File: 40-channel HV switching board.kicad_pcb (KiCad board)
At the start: 2 copper layers, 83.8 x 121.9 mm, 210 parts, among them IC1 ATMEG328PU, J1 CONN_4, J2 CONN_10, J3 CONN_2, J4 CONN_2, J5 CONN_40, P1 CONN_6, P2 CONN_6, SW1 DPST, U1 74HC595A, U2 74HC595A, U3 74HC595A, U4 74HC595A, U5 74HC595A, U6 7400, X1 16MHz

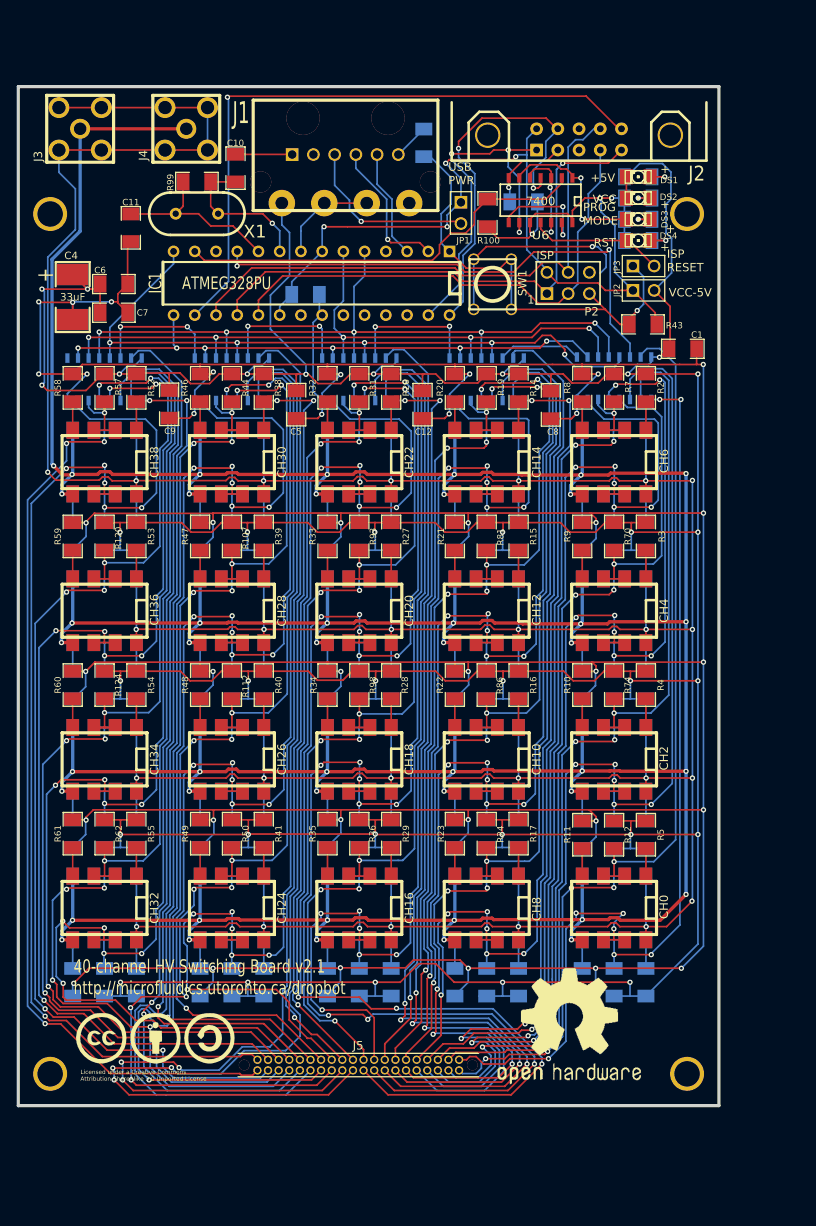
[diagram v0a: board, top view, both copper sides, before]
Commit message: Update to work with KiCad 4.0
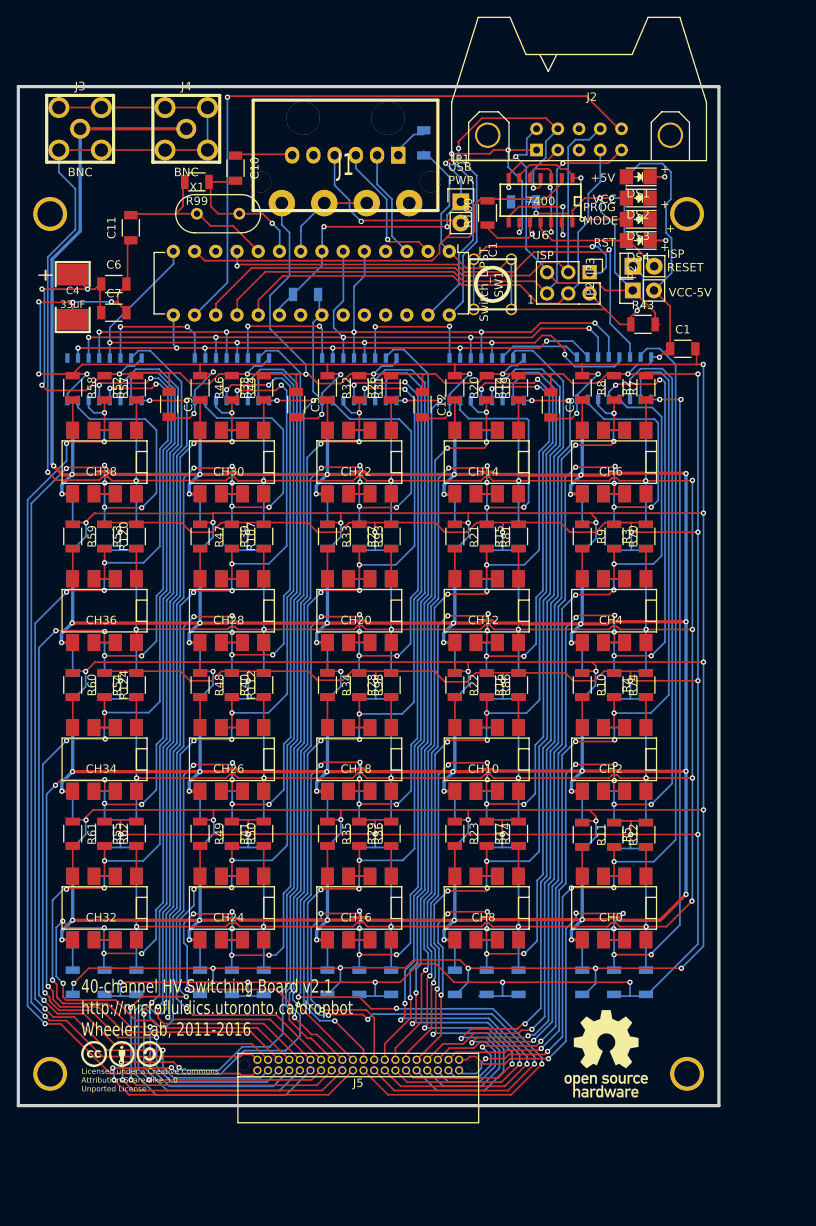
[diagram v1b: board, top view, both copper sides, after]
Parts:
- removed the G*** at (33.0, 129.1)
- removed the G*** at (72.9, 118.4)
- added G***: LOGO, footprints:OSHW_logo_10mm, F.Cu at (86.8, 130.9)
- added G***: LOGO, footprints:CC_S_A_logo_10mm, F.Cu at (28.9, 130.9)
- C1, C10, C11, C12, C13, C14, C3, C5, C6, C7, C8, C9: footprint SM1206 -> Capacitors_SMD:C_1206
- C2, C4: footprint SM2917 -> footprints:SM2917
- CH0, CH1, CH10, CH11, CH12, CH13, CH14, CH15, CH16, CH17, CH18, CH19, CH2, CH20, CH21, CH22, CH23, CH24, CH25, CH26, CH27, CH28, CH29, CH3, CH30, CH31, CH32, CH33, CH34, CH35, CH36, CH37, CH38, CH39, CH4, CH5, CH6, CH7, CH8, CH9: footprint 8DIPCMS -> SMD_Packages:DIP-8_SMD
- DS1, DS2, DS3, DS4: footprint LED-1206 -> LEDs:LED_1206
- IC1: footprint DIP-28 -> Housings_DIP:DIP-28_W7.62mm
- J1: value CONN_4 -> CONN_01X04; footprint Molex_15-24-4441 -> footprints:Molex_15-24-4441
- J2: value CONN_10 -> CONN_01X10; footprint HE10-10C -> Connect:HE10-10C
- J3, J4: value CONN_2 -> BNC; footprint JACK_SMA -> footprints:JACK_SMA
- J5: value CONN_40 -> CONN_01X40; footprint TFML-120-01-XXX-D-RA -> footprints:TFML-120-01-XXX-D-RA
- JP1, JP2, JP3: footprint PIN_ARRAY_2X1 -> Pin_Headers:Pin_Header_Straight_1x02
- P1: value CONN_6 -> CONN_01X06; footprint PIN_ARRAY-6X1 -> Pin_Headers:Pin_Header_Angled_1x06
- P2: value CONN_6 -> CONN_01X06; footprint pin_array_3x2 -> Pin_Headers:Pin_Header_Straight_2x03
- R1, R10, R100, R101, R102, R103, R104, R105, R106, R107, R108, R109, R11, R110, R111, R112, R113, R114, R115, R116, R117, R118, R119, R12, R120, R121, R122, R123, R124, R125, R126, R127, R13, R14, R15, R16, R17, R18, R19, R2, R20, R21, R22, R23, R24, R25, R26, R27, R28, R29, R3, R30, R31, R32, R33, R34, R35, R36, R37, R38, R39, R4, R40, R41, R42, R43, R44, R45, R46, R47, R48, R49, R5, R50, R51, R52, R53, R54, R55, R56, R57, R58, R59, R6, R60, R61, R62, R63, R64, R65, R66, R67, R68, R69, R7, R70, R71, R72, R73, R74, R75, R76, R77, R78, R79, R8, R80, R81, R82, R83, R84, R85, R86, R87, R88, R89, R9, R90, R91, R92, R93, R94, R95, R96, R97, R98, R99: footprint SM1206 -> Resistors_SMD:R_1206
- SW1: value DPST -> Switch_DPST; footprint SW_PUSH_6mm -> footprints:SW_PUSH_6mm
- U1, U2, U3, U4, U5: footprint SO16E -> footprints:SO16E
- U6: footprint SO14E -> footprints:SO14E
- X1: footprint HC-49V -> Crystals:HC-49V
- moved IC1 16.9 mm to (68.1, 35.0), turned to 270 degrees
- moved P1 6.35 mm to (62.0, 23.4), turned to 90 degrees
- moved P2 2.86 mm to (84.8, 37.5), turned to 270 degrees
- moved JP1 1.33 mm to (69.5, 29.0), turned to 0 degrees
- moved JP2 1.29 mm to (90.0, 39.6), turned to 90 degrees
- moved JP3 1.26 mm to (90.0, 36.7), turned to 90 degrees
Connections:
- C3 pad 1: N-00000115 -> Net-(C3-Pad1)
- IC1 pad 12: (no net) -> Net-(IC1-Pad12)
- IC1 pad 21: (no net) -> Net-(IC1-Pad21)
- IC1 pad 23: (no net) -> Net-(IC1-Pad23)
- IC1 pad 24: (no net) -> Net-(IC1-Pad24)
- IC1 pad 25: (no net) -> Net-(IC1-Pad25)
- IC1 pad 26: (no net) -> Net-(IC1-Pad26)
- IC1 pad 4: (no net) -> Net-(IC1-Pad4)
- J1 pad 1: (no net) -> Net-(J1-Pad1)
- J2 pad 5: (no net) -> Net-(J2-Pad5)
- J2 pad 6: (no net) -> Net-(J2-Pad6)
- J3 pad 1: HVGND -> HV
- J3 pad 2: HV -> HVGND
- J4 pad 1: HVGND -> HV
- J4 pad 2: HV -> HVGND
- P1 pad 1: GND -> Net-(C3-Pad1)
- P1 pad 2: (no net) -> RX
- P1 pad 3: +5V_USB -> TX
- P1 pad 4: TX -> +5V_USB
- P1 pad 5: RX -> Net-(P1-Pad5)
- P1 pad 6: N-00000115 -> GND
- P2 pad 1: D12/MISO -> GND
- P2 pad 2: VCC -> RST
- P2 pad 3: D13/SCK -> D11/MOSI
- P2 pad 4: D11/MOSI -> D13/SCK
- P2 pad 5: RST -> VCC
- P2 pad 6: GND -> D12/MISO
- U5 pad 9: (no net) -> Net-(U5-Pad9)
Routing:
- net Net-(C3-Pad1): track 0.00 -> 4.44 mm
- net N-00000115: track 4.31 -> 0.00 mm
- net D7: track 50.3 -> 52.1 mm
- net VCC: track 126.4 -> 125.4 mm, vias 7 -> 8
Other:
- board text added: "40-channel HV Switching Board v2.1 http://microfluidics.utoronto.ca/dropbot Wheeler Lab, 2011-2016"
- board text removed: "40-channel HV Switching Board v2.1 http://microfluidics.utoronto.ca/dropbot"

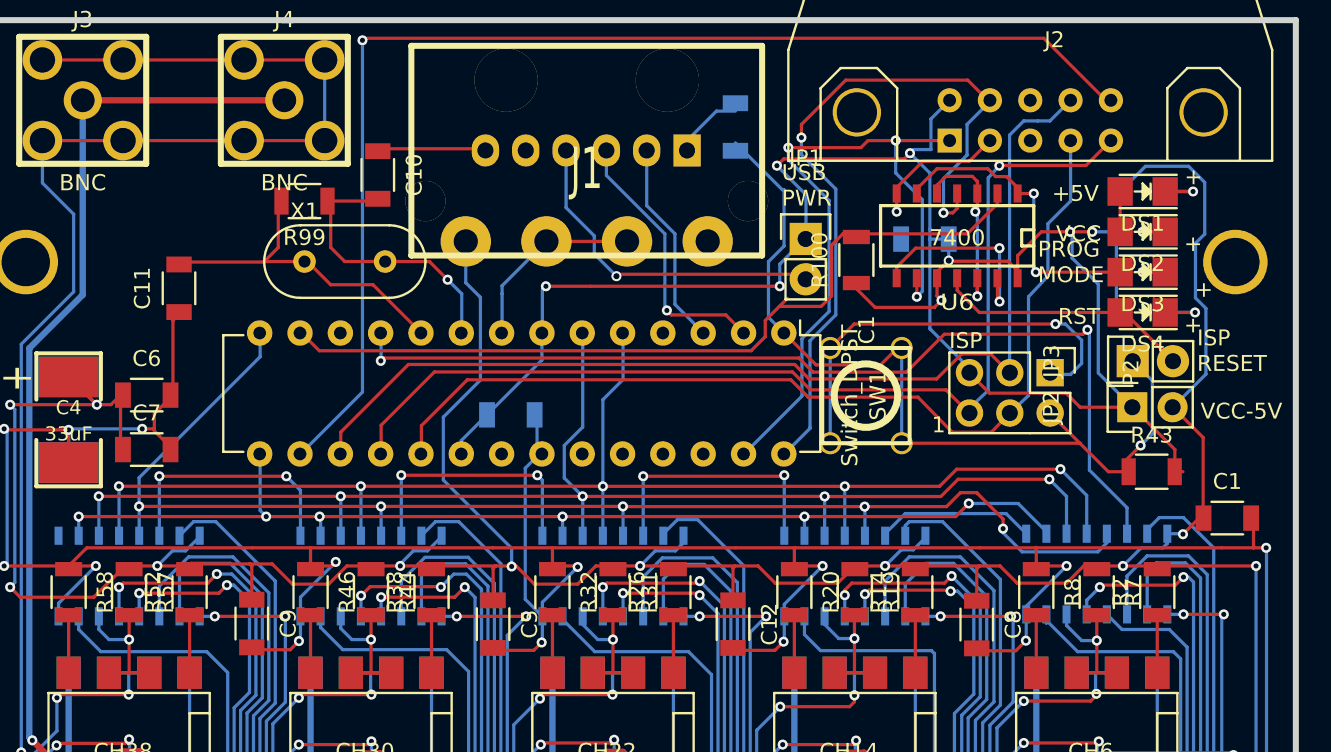
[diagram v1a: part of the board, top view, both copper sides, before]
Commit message: [WIP] Switch caps and LEDs to 0805 footprints
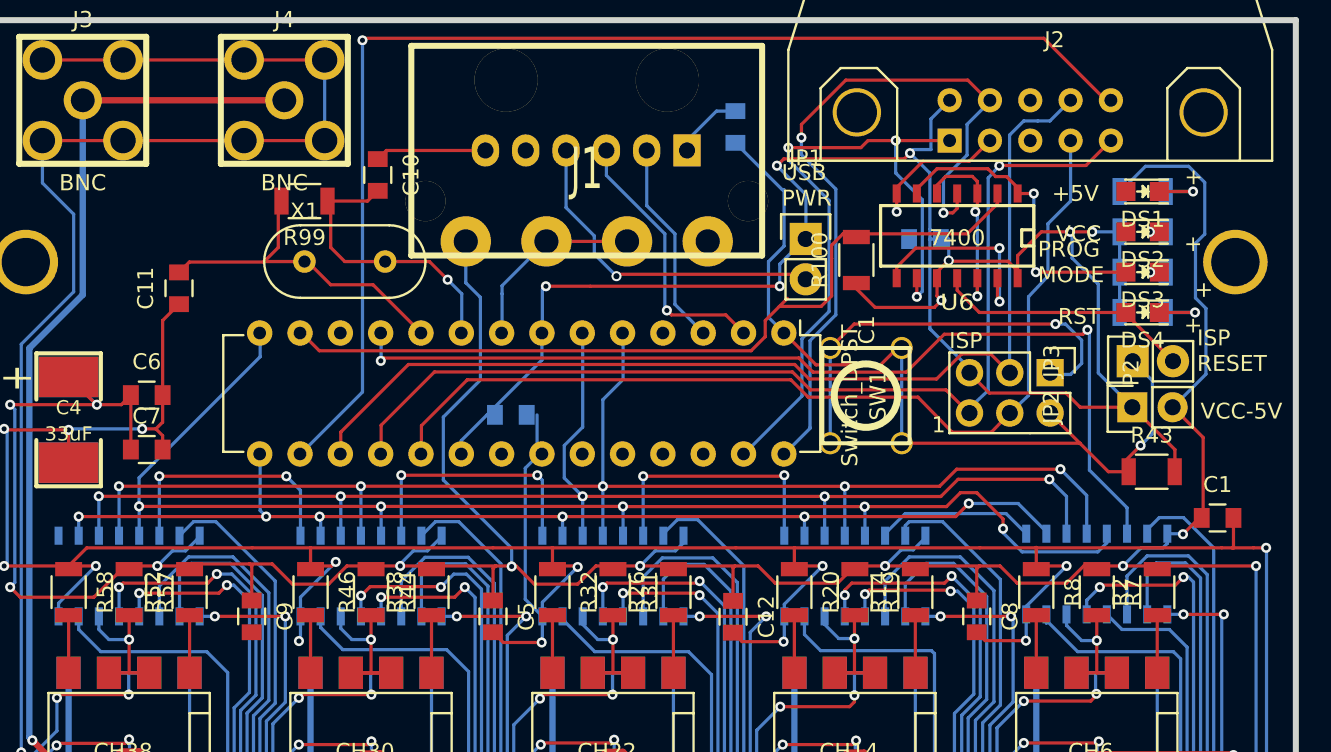
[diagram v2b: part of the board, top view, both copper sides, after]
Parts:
- C1, C10, C11, C12, C13, C14, C3, C5, C6, C7, C8, C9: footprint Capacitors_SMD:C_1206 -> Capacitors_SMD:C_0805
- DS1, DS2, DS3, DS4: footprint LEDs:LED_1206 -> LEDs:LED_0805
- moved C1 0.61 mm to (95.4, 46.6)
- moved C8 0.51 mm to (80.2, 52.8)
- moved C5 0.49 mm to (49.8, 52.8)
- moved C12 0.46 mm to (64.9, 52.8)
- moved C9 0.45 mm to (34.5, 52.8)
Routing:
- net GND: track 728.0 -> 723.0 mm
- net Net-(DS3-Pad1): track 3.07 -> 1.56 mm
- net Net-(DS2-Pad1): track 3.07 -> 1.61 mm
- net +5V: track 712.6 -> 714.0 mm

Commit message: [WIP] Add sci-bots logo
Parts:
- added G***: LOGO, LOGO, F.Cu at (34.0, 120.9)
- moved G*** 0.83 mm to (28.8, 131.8)
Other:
- board text added: "40-channel HV Switching Board v2.1 http://sci-bots.com Sci-Bots Inc., 2016"
- board text removed: "40-channel HV Switching Board v2.1 http://microfluidics.utoronto.ca/dropbot Wheeler Lab, 2011-2016"

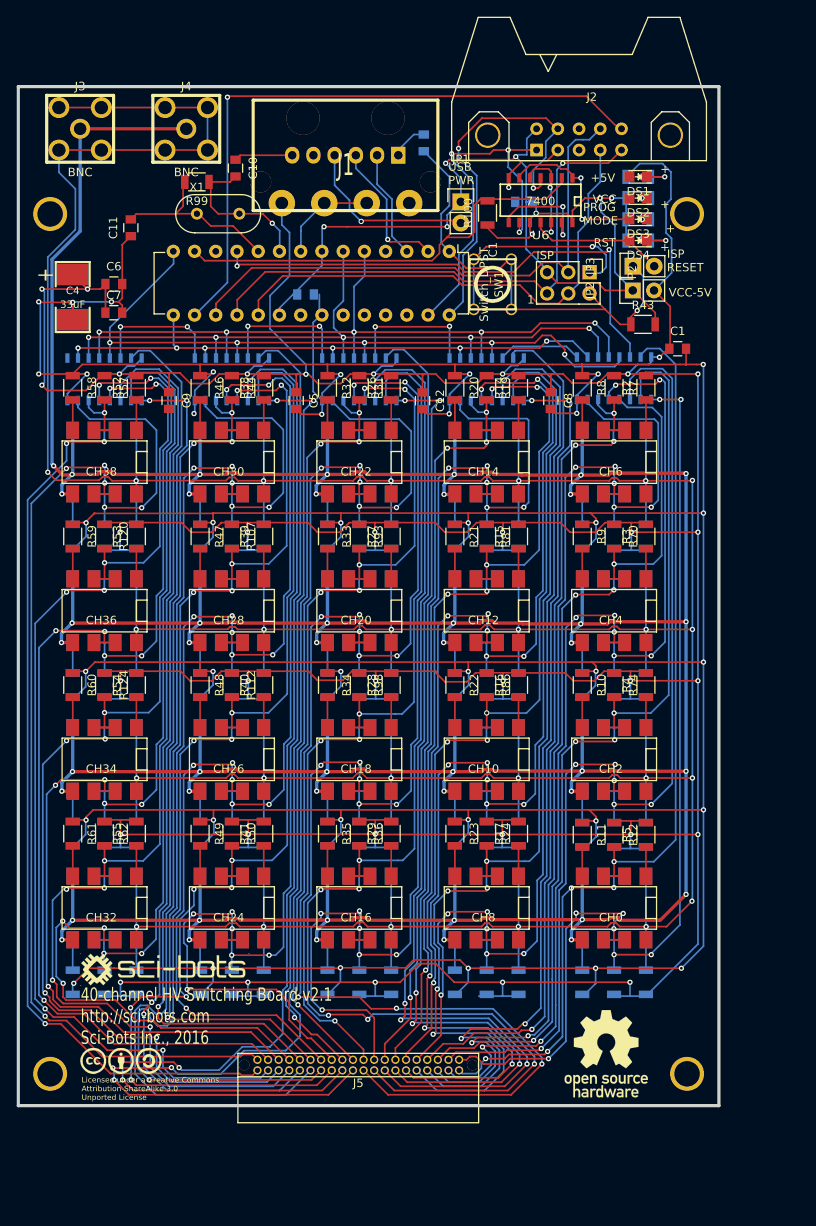
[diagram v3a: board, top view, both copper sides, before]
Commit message: [WIP] Fix placement of crystal, bump version to 2.1.1
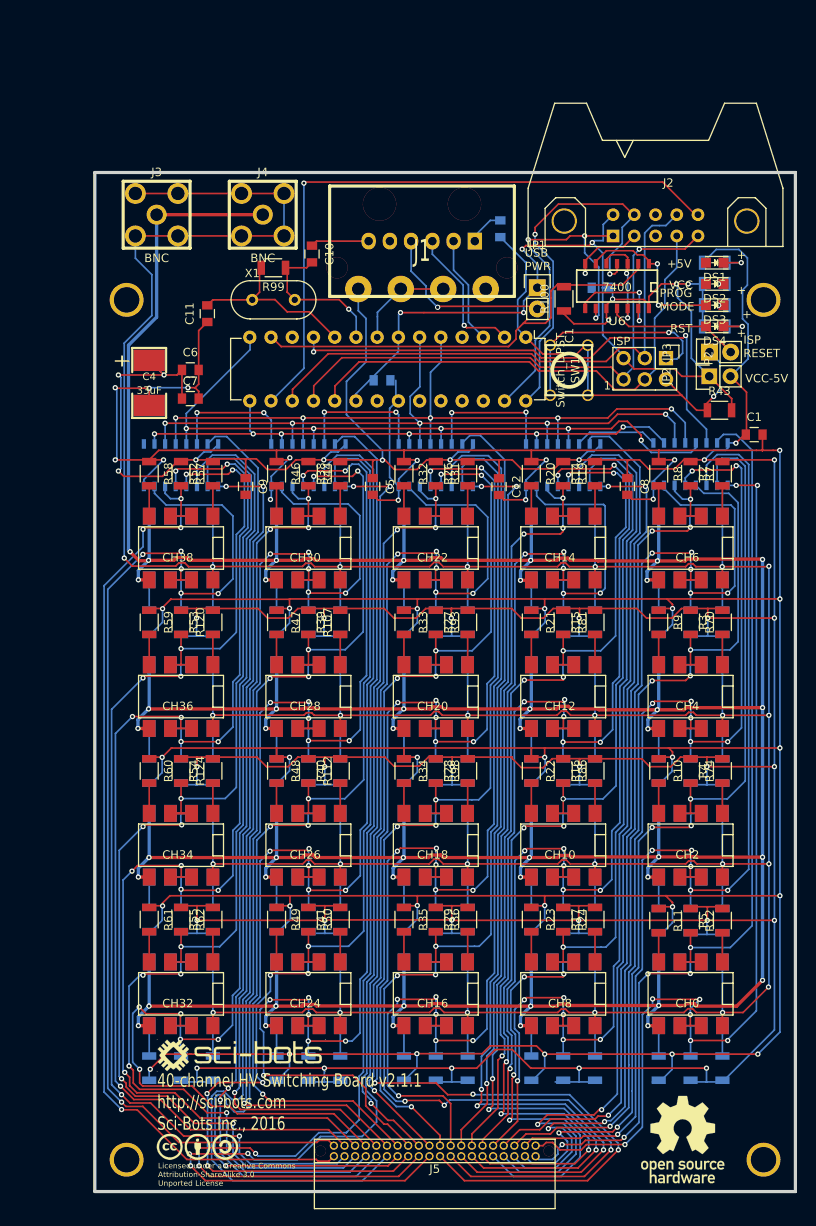
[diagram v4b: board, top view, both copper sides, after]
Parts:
- moved 1PIN 13.8 mm to (105.7, 143.6)
- moved C8 13.8 mm to (89.4, 63.1)
- moved C9 13.8 mm to (43.7, 63.1)
- moved CH0 13.8 mm to (96.9, 123.8)
- moved CH1 13.8 mm to (96.9, 123.8)
- moved CH10 13.8 mm to (81.7, 106.0)
- moved CH11 13.8 mm to (81.7, 106.0)
- moved CH2 13.8 mm to (96.9, 106.0)
- moved CH3 13.8 mm to (96.9, 106.0)
- moved CH8 13.8 mm to (81.7, 123.8)
- moved CH9 13.8 mm to (81.7, 123.8)
- moved G*** 13.8 mm to (96.0, 141.2)
- moved R103 13.8 mm to (55.0, 114.9)
- moved R13 13.8 mm to (81.7, 114.9)
- moved R14 13.8 mm to (85.5, 61.6)
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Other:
- board text added: "40-channel HV Switching Board v2.1.1 http://sci-bots.com Sci-Bots Inc., 2016"
- board text removed: "40-channel HV Switching Board v2.1 http://sci-bots.com Sci-Bots Inc., 2016"
